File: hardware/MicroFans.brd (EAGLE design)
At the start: 100 x 80 mm, 29 parts, among them IC4 ATMEGA328P, IC7 OPA4251UA, J1 COMPUTER-PERIPHERAL-POWERVERT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, Y1 20Mhz

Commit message: Update board
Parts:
- added C3: 1uF, SparkFun-Capacitors:0805
- added C7: 0.1uF, SparkFun-Passives:1206
- added D1, D2: 3V6, SparkFun-DiscreteSemi:SOD-323
- added IC1: (no value), SparkFun-PowerIC:SOT223
- added JP7: (no value), SparkFun-Connectors:MOLEX-1X3
- added R10: 47K, SparkFun-Passives:0805
- added R11, R8: 8K6, SparkFun-Resistors:1206
- added R12, R9: 2K2, SparkFun-Resistors:1206
- added R13: 1K5, SparkFun-Passives:1206
- added R14, R15: 68, SparkFun-Passives:1206
- added R16: 220, SparkFun-Resistors:1206
- C1, C2: device SparkFun-Capacitors:CAP-PTH-SMALL-KIT -> SparkFun-Capacitors:0805
- C4: value 0.1uF -> 1uF; device SparkFun-Capacitors:CAP-PTH-SMALL-KIT -> SparkFun-Capacitors:0805
- C5, C6: device SparkFun-Capacitors:CAP-PTH-SMALL-KIT -> SparkFun-Passives:1206
- J1: value COMPUTER-PERIPHERAL-POWERVERTICAL -> (none)
- JP1: value USB-A-S -> USB-A-SMD; device SparkFun-Connectors:USB-A-S -> SparkFun-Connectors:USB-A-S-NOSILK-FEMALE
- R1: device SparkFun-Resistors:1206 -> SparkFun-Passives:0805
- R4: value 220 -> 47K; device SparkFun-Resistors:1206 -> SparkFun-Passives:0805
- R6: value 47K -> 2K2
- R7: value 2K2 -> 47K; device SparkFun-Resistors:1206 -> SparkFun-Passives:0805
- Y1: value 20Mhz -> 16MHZ
- moved R6 190.1 mm to (44.5, 38.1)
- moved R5 188.4 mm to (10.2, 55.9), turned to 90 degrees
- moved C1 186.7 mm to (41.9, 31.8)
- moved R7 179.5 mm to (26.7, 27.9), turned to 180 degrees
- moved JP5 152.2 mm to (39.4, 3.81)
- moved IC7 149.3 mm to (38.7, 24.8), turned to 90 degrees
- moved JP4 141.7 mm to (30.5, 3.81)
- moved C4 135.2 mm to (44.5, 48.3), turned to 90 degrees
- moved JP3 131.4 mm to (21.6, 3.81)
- moved IC3 125.6 mm to (41.9, 12.7)
- moved IC5 124.8 mm to (33.0, 12.7)
- moved IC6 124.0 mm to (24.1, 12.7)
- moved Y1 119.6 mm to (31.8, 40.6)
- moved C6 115.7 mm to (17.1, 26.0), turned to 270 degrees
- moved C5 114.3 mm to (14.0, 31.8), turned to 270 degrees
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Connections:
- removed net +25V: IC5.3
- removed net FAN1_TACH: JP5.3
- removed net FAN2_TACH: JP4.3
- removed net FAN3_TACH: JP3.3
- removed net V+: IC7.4
- removed net V-: IC7.11
- new net +12V: IC1.3, IC3.3, IC5.3, IC6.3, IC7.4, J1.12V
- new net N$1: IC1.2, JP7.2
- new net N$19: IC6.1, IC7.14, R8.1
- new net N$20: IC7.13, R8.2, R9.1
- new net N$21: C3.1, IC7.12, R7.1
- new net N$22: IC7.9, R11.2, R12.1
- new net N$23: IC4.25, R7.2
- new net N$24: C4.1, IC7.10, R10.1
- new net N$25: IC1.1, IC7.8, R11.1
- new net N$26: D1.1, JP1.D-, R13.2, R15.1
- new net N$27: JP1.VBUS
- new net N$28: D2.1, JP1.D+, R14.1
- new net N$29: IC4.32, R14.2
- new net N$30: IC4.1, R15.2
- new net N$33: J1.5V, R16.2
- new net N$34: IC4.26, R10.2
- new net SENSE1: IC4.12, JP5.3
- new net SENSE2: IC4.13, JP4.3
- new net SENSE3: IC4.14, JP3.3
- new net SENSE4: IC4.11, JP7.3
- net +5V: now also C7.1, R13.1; no longer C4.1, J1.5V, R4.2
- net GND: now also C1.2, C2.2, C3.2, C7.2, D1.2, D2.2, IC7.11, JP1.GND, JP7.1, R12.2, R6.2, R9.2; no longer R7.2
- net N$12: now also IC4.24, R4.2; no longer R6.2
- net N$13: now also IC6.2, JP3.2; no longer JP4.2
- net N$15: now also C1.1; no longer C2.1
- net N$16: now also R3.1; no longer C2.2, R7.1
- net N$17: now also C2.1, R4.1; no longer C1.1, R6.1
- net N$18: now also R6.1; no longer C1.2, R3.1
- net N$5: now also IC4.23
- net N$7: now also R16.1; no longer R4.1
- net N$8: now also IC5.2, JP4.2; no longer JP3.2
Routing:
- net +12V: track 0.00 -> 48.0 mm
- net N$2: track 0.00 -> 13.0 mm, vias 0 -> 1
- net SENSE2: track 0.00 -> 11.6 mm
- net SENSE4: track 0.00 -> 11.6 mm
- net SENSE3: track 0.00 -> 11.6 mm
- net SENSE1: track 0.00 -> 11.6 mm
- net GND: track 0.00 -> 7.22 mm, vias 0 -> 3
- net N$8: track 0.00 -> 5.79 mm
- net N$31: track 0.00 -> 5.79 mm
- net N$13: track 0.00 -> 5.79 mm
- net N$1: track 0.00 -> 5.79 mm
- net N$28: track 0.00 -> 5.52 mm
- net N$26: track 0.00 -> 5.52 mm
- net N$7: track 0.00 -> 3.22 mm
- net N$17: track 0.00 -> 2.01 mm
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- added copper zone on layer 16, net GND
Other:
- board size 100 x 80 mm -> 57.1 x 38.1 mm

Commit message: More work on board
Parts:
- removed IC7: OPA4251UA, linear:SO14
- added IC2: (no value), SparkFun-PowerIC:SOT223
- added R17, R18, R19, R20: 10K, SparkFun-Resistors:0805
- C5, C6: device SparkFun-Passives:1206 -> SparkFun-Capacitors:0805
- IC4: value ATMEGA328P -> (none); device SparkFun-DigitalIC:TQFP32-08 -> SparkFun-PowerIC:SOT223
- IC5: value (none) -> ATMEGA328P; device SparkFun-PowerIC:SOT223 -> SparkFun-DigitalIC:TQFP32-08
- IC6: value (none) -> OPA4251UA; device SparkFun-PowerIC:SOT223 -> linear:SO14
- R1, R10, R4, R7: device SparkFun-Passives:0805 -> SparkFun-Resistors:0805
- R11, R12, R16, R2, R3, R5, R6, R8, R9: device SparkFun-Resistors:1206 -> SparkFun-Resistors:0805
- R13, R14, R15: device SparkFun-Passives:1206 -> SparkFun-Resistors:0805
- moved R15 80.3 mm to (13.3, 21.0), turned to 0 degrees
- moved R14 77.7 mm to (13.3, 18.4), turned to 0 degrees
- moved R13 55.9 mm to (13.3, 23.5), turned to 180 degrees
- moved R5 49.5 mm to (37.5, 14.6), turned to 270 degrees
- moved R12 46.6 mm to (19.7, 11.4), turned to 270 degrees
- moved R9 44.5 mm to (28.6, 11.4), turned to 270 degrees
- moved R8 41.4 mm to (28.6, 14.6), turned to 270 degrees
- moved PWR 41.3 mm to (48.9, 34.3), turned to 90 degrees
- moved R11 39.6 mm to (19.7, 14.6), turned to 270 degrees
- moved R16 35.7 mm to (46.4, 31.8)
- moved R6 27.6 mm to (37.5, 11.4), turned to 270 degrees
- moved IC4 23.3 mm to (41.9, 12.7), turned to 0 degrees
- moved Y1 23.3 mm to (10.2, 31.8), turned to 90 degrees
- moved C3 21.2 mm to (29.8, 34.9)
- moved C4 17.6 mm to (33.0, 34.9)
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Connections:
- net N$26 renamed D-
- net N$28 renamed D+
- removed net N$4: ICSP.5
- net +12V: now also IC2.3, IC4.3, IC6.4; no longer IC5.3, IC6.3, IC7.4
- net +5V: now also IC5.18, IC5.4, IC5.6, R17.1, R18.1, R19.1, R20.1; no longer IC4.18, IC4.4, IC4.6
- net GND: now also IC5.21, IC5.3, IC5.5, IC6.11; no longer IC4.21, IC4.3, IC4.5, IC7.11
- net N$10: now also IC5.17
- net N$11: now also IC5.15
- net N$12: now also IC5.24; no longer IC4.24
- net N$13: now also IC2.2; no longer IC6.2
- net N$14: now also IC3.1, IC6.7; no longer IC5.1, IC7.7
- net N$15: now also IC6.3; no longer IC7.3
- net N$16: now also IC6.2; no longer IC7.2
- net N$17: now also IC6.5; no longer IC7.5
- net N$18: now also IC6.6; no longer IC7.6
- net N$19: now also IC2.1, IC6.14; no longer IC6.1, IC7.14
- net N$2: now also IC4.1, IC6.1; no longer IC3.1, IC7.1
- net N$20: now also IC6.13; no longer IC7.13
- net N$21: now also IC6.12; no longer IC7.12
- net N$22: now also IC6.9; no longer IC7.9
- net N$23: now also IC5.25; no longer IC4.25
- net N$24: now also IC6.10; no longer IC7.10
- net N$25: now also IC6.8; no longer IC7.8
- net N$29: now also IC5.32; no longer IC4.32
- net N$3: now also IC5.16
- net N$30: now also IC5.1; no longer IC4.1
- net N$31: now also IC4.2; no longer IC3.2
- net N$34: now also IC5.26; no longer IC4.26
- net N$5: now also IC5.23; no longer IC4.23
- net N$6: now also IC5.7; no longer IC4.7
- net N$8: now also IC3.2; no longer IC5.2
- net N$9: now also IC5.8; no longer IC4.8
- net RESET: now also IC5.29, ICSP.5; no longer IC4.29
- net SENSE1: now also IC5.12, R17.2; no longer IC4.12
- net SENSE2: now also IC5.13, R18.2; no longer IC4.13
- net SENSE3: now also IC5.14, R19.2; no longer IC4.14
- net SENSE4: now also IC5.11, R20.2; no longer IC4.11
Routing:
- net N$25: track 0.00 -> 37.3 mm, vias 0 -> 2
- net GND: track 7.22 -> 42.8 mm, vias 3 -> 11
- net +12V: track 48.0 -> 78.0 mm
- net N$14: track 0.00 -> 28.9 mm, vias 0 -> 2
- net N$22: track 0.00 -> 27.1 mm, vias 0 -> 2
- net N$33: track 0.00 -> 24.7 mm, vias 0 -> 1
- net +5V: track 0.00 -> 21.6 mm, vias 0 -> 2
- net N$5: track 0.00 -> 21.4 mm, vias 0 -> 2
- net N$18: track 0.00 -> 21.3 mm, vias 0 -> 2
- net N$6: track 0.00 -> 21.0 mm
- net N$19: track 0.00 -> 20.8 mm
- net SENSE3: track 11.6 -> 30.3 mm
- net N$15: track 2.01 -> 20.3 mm, vias 0 -> 2
- net N$24: track 0.00 -> 18.1 mm
- net N$21: track 0.00 -> 17.5 mm
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
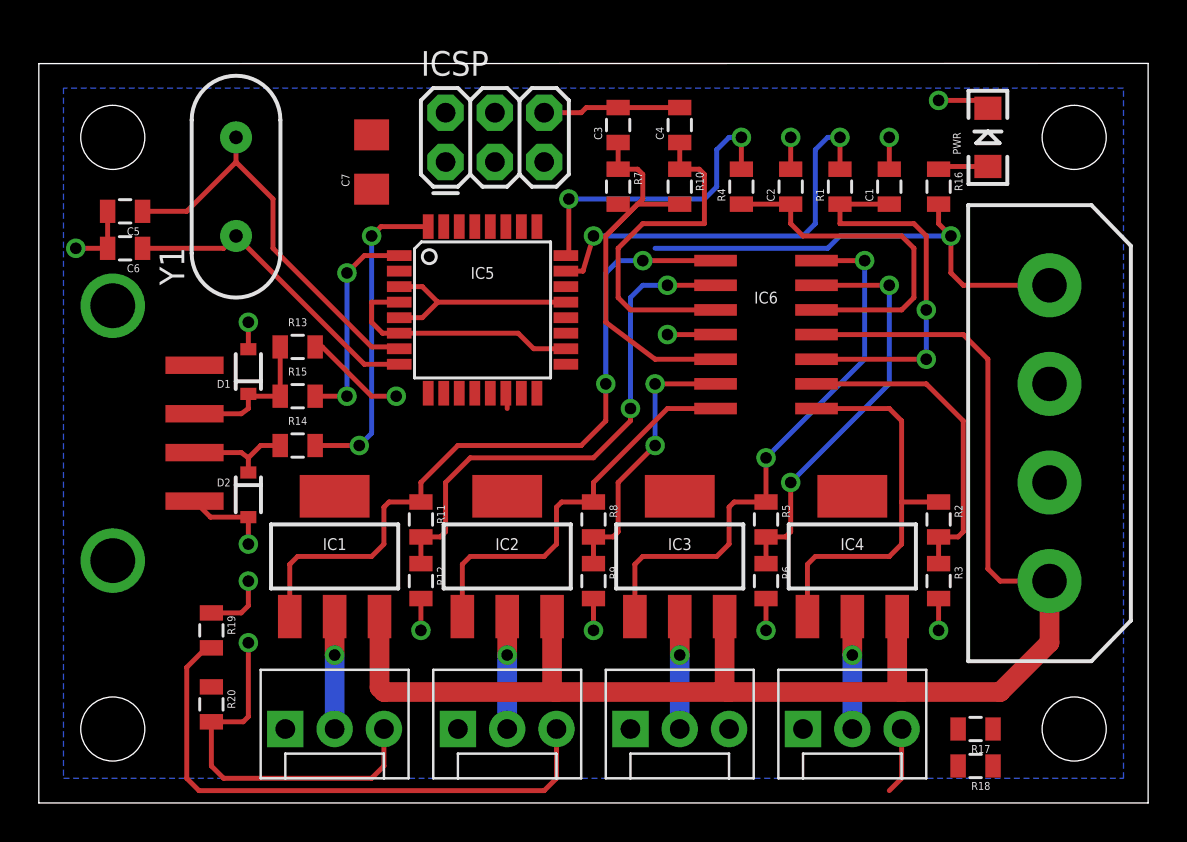
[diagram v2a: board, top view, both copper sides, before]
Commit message: Updated board with LM2341
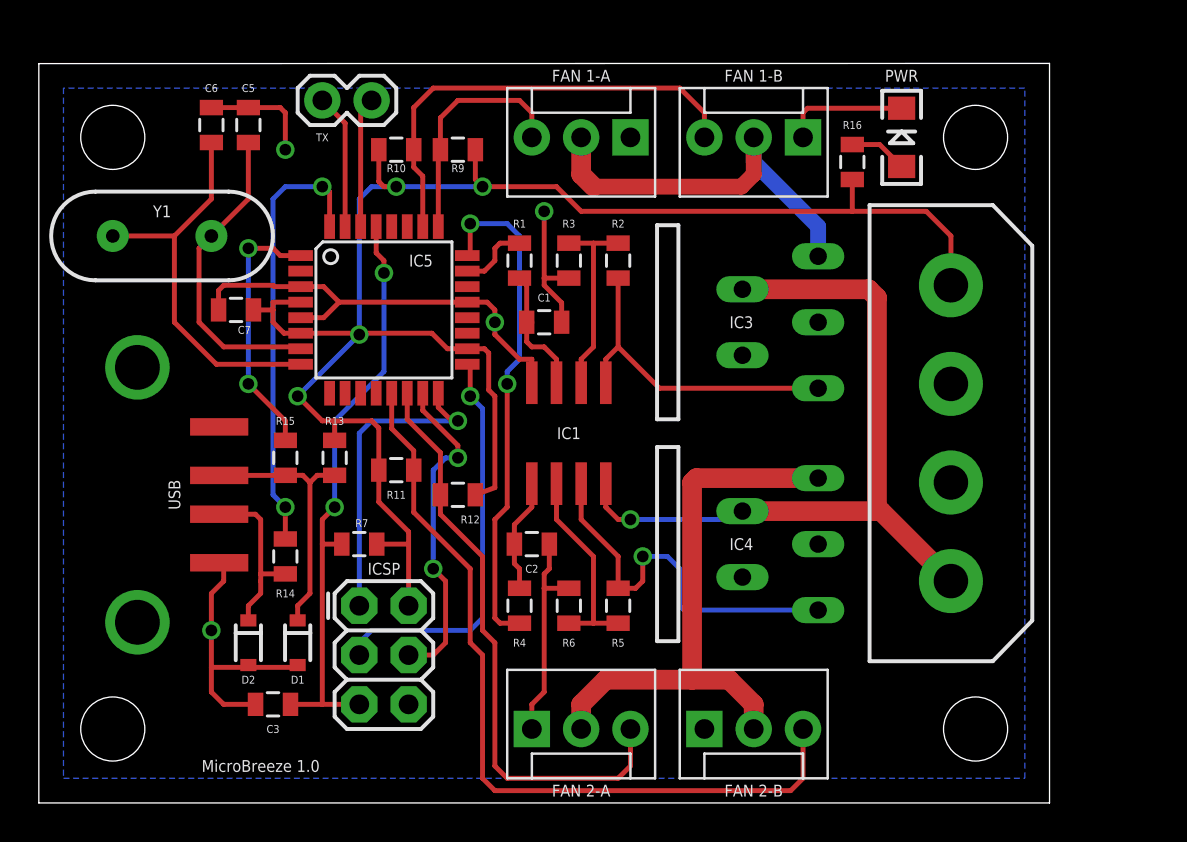
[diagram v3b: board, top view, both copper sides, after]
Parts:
- removed C4: 1uF, SparkFun-Capacitors:0805
- removed IC2: (no value), SparkFun-PowerIC:SOT223
- removed IC6: OPA4251UA, linear:SO14
- removed JP6, JP8: STAND-OFF, SparkFun:STAND-OFF
- removed JP7: (no value), SparkFun-Connectors:MOLEX-1X3
- removed R17, R18, R19, R20: 10K, SparkFun-Resistors:0805
- removed R8: 8K6, SparkFun-Resistors:0805
- added HOLE2, HOLE3, HOLE4: STAND-OFF, SparkFun:STAND-OFF
- added USB: USB-A-SMD, SparkFun-Connectors:USB-A-S-NOSILK-FEMALE
- C3: value 1uF -> 0.1uF
- C7: device SparkFun-Passives:1206 -> SparkFun-Capacitors:0805
- IC1: value (none) -> OPA2251UA; device SparkFun-PowerIC:SOT223 -> linear:SO08
- IC3, IC4: value (none) -> LM2941TO220-V; device SparkFun-PowerIC:SOT223 -> lm2941:TO220-51
- JP1: value USB-A-SMD -> (none); device SparkFun-Connectors:USB-A-S-NOSILK-FEMALE -> SparkFun-Connectors:MOLEX-1X3
- JP2: value STAND-OFF -> (none); device SparkFun:STAND-OFF -> SparkFun-Connectors:MOLEX-1X3
- JP5: device SparkFun-Connectors:MOLEX-1X3 -> SparkFun-Connectors:1X02
- R10, R7: value 47K -> 10K
- R11: value 8K6 -> 10K
- R12, R9: value 2K2 -> 10K
- moved JP5 39.3 mm to (17.1, 36.2), turned to 180 degrees
- moved JP2 35.6 mm to (39.4, 34.3), turned to 180 degrees
- moved C3 34.7 mm to (12.1, 5.08), turned to 180 degrees
- moved JP1 30.7 mm to (30.5, 34.3), turned to 180 degrees
- moved R3 25.2 mm to (27.3, 27.9)
- moved R4 24.4 mm to (24.8, 10.2), turned to 270 degrees
- moved R9 23.3 mm to (21.6, 33.7), turned to 180 degrees
- moved ICSP 23.3 mm to (16.5, 10.2), turned to 270 degrees
- moved C2 22.7 mm to (25.4, 13.3), turned to 0 degrees
- moved R7 22.7 mm to (16.5, 13.3), turned to 180 degrees
- moved R2 21.2 mm to (29.8, 27.9), turned to 90 degrees
- moved C1 19.1 mm to (26.0, 24.8), turned to 0 degrees
- moved R1 16.9 mm to (24.8, 27.9)
- moved R10 14.7 mm to (18.4, 33.7), turned to 0 degrees
- moved D1 14.2 mm to (13.3, 8.26), turned to 270 degrees
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- renumbered JP9 to HOLE1
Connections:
- removed net N$19: IC2.1, IC6.14, R8.1
- removed net N$20: IC6.13, R8.2, R9.1
- removed net N$21: C3.1, IC6.12, R7.1
- removed net N$22: IC6.9, R11.2, R12.1
- removed net N$23: IC5.25, R7.2
- removed net N$24: C4.1, IC6.10, R10.1
- removed net N$25: IC1.1, IC6.8, R11.1
- removed net N$27: JP1.VBUS
- removed net N$31: IC4.2, JP5.2
- removed net N$33: J1.5V, R16.2
- removed net N$34: IC5.26, R10.2
- new net N$4: IC5.31, JP5.2
- net +12V: now also IC1.8, IC3.4, IC4.4; no longer IC1.3, IC2.3, IC3.3, IC4.3, IC6.4
- net +5V: now also J1.5V, R10.1, R11.1, R12.1, R16.2, R7.1, R9.1; no longer R17.1, R18.1, R19.1, R20.1
- net D+: now also USB.D+; no longer JP1.D+
- net D-: now also USB.D-; no longer JP1.D-
- net GND: now also IC1.4, IC3.2, IC3.3, IC4.2, IC4.3, JP1.1, JP2.1, USB.GND; no longer C4.2, IC6.11, JP1.GND, JP5.1, JP7.1, R12.2, R9.2
- net N$1: now also IC5.30, JP5.1; no longer IC1.2, JP7.2
- net N$13: now also IC4.5, JP4.2; no longer IC2.2
- net N$14: now also IC1.7, IC4.1; no longer IC3.1, IC6.7
- net N$15: now also IC1.3; no longer IC6.3
- net N$16: now also IC1.2; no longer IC6.2
- net N$17: now also IC1.5; no longer IC6.5
- net N$18: now also IC1.6; no longer IC6.6
- net N$2: now also IC1.1, IC3.1; no longer IC4.1, IC6.1
- net N$8: now also IC3.5, JP1.2, JP2.2; no longer IC3.2, JP4.2
- net RESET: now also C3.1, R7.2
- net SENSE1: now also IC5.25, JP1.3, R9.2; no longer IC5.12, JP5.3, R17.2
- net SENSE2: now also IC5.26, JP2.3, R10.2; no longer IC5.13, JP4.3, R18.2
- net SENSE3: now also IC5.13, R11.2; no longer IC5.14, R19.2
- net SENSE4: now also IC5.14, JP4.3, R12.2; no longer IC5.11, JP7.3, R20.2
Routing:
- net +5V: track 21.6 -> 92.9 mm, vias 2 -> 4
- net +12V: track 78.0 -> 39.0 mm, vias 0 -> 1
- net N$25: track 37.3 -> 0.00 mm, vias 2 -> 0
- net RESET: track 0.00 -> 30.6 mm, vias 0 -> 2
- net N$22: track 27.1 -> 0.00 mm, vias 2 -> 0
- net GND: track 42.8 -> 68.1 mm, vias 11 -> 4
- net N$33: track 24.7 -> 0.00 mm, vias 1 -> 0
- net SENSE2: track 0.00 -> 23.5 mm
- net N$13: track 5.79 -> 29.2 mm, vias 1 -> 0
- net N$10: track 0.00 -> 20.9 mm, vias 0 -> 1
- net N$19: track 20.8 -> 0.00 mm
- net N$24: track 18.1 -> 0.00 mm
- net N$5: track 21.4 -> 3.66 mm, vias 2 -> 0
- net N$21: track 17.5 -> 0.00 mm
- net N$11: track 0.00 -> 16.9 mm, vias 0 -> 2
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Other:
- board size 57.1 x 38.1 mm -> 52.1 x 38.1 mm
- board text added: "FAN 1-A"
- board text added: "FAN 1-B"
- board text added: "FAN 2-A"
- board text added: "FAN 2-B"
- board text added: "MicroBreeze 1.0"
- board text added: "TX"
